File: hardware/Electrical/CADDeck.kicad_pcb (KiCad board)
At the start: 2 copper layers, 129 x 82.1 mm, 44 parts, among them J1 Conn_01x05_Socket, J4 Conn_01x04_Socket, J5 Conn_01x10_Socket, Q1 2N2222, SW1 SW_Push, SW10 SW_Push, SW2 SW_Push, SW3 SW_Push, SW4 SW_Push, SW5 SW_Push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

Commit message: Platine Optimiert
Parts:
- moved R11 97.1 mm to (87.9, 92.5)
- moved R12 81.9 mm to (87.9, 90.6), turned to 0 degrees
- renumbered J1 to J1_Knob, J4 to J4_Joystick, J5 to J5_WT32_SC01
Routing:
- net Net-(J5-Pin_10): track 123.8 -> 131.4 mm
- net Net-(J5-Pin_8): track 119.7 -> 126.0 mm
- net Net-(U1-P05): track 58.0 -> 63.6 mm
- net +3.3V: track 344.0 -> 346.0 mm
- net Net-(J5-Pin_7): track 131.7 -> 132.7 mm
- net Net-(J1-Pin_3): track 108.2 -> 107.3 mm
- net Net-(U1-P11): track 91.6 -> 92.3 mm
- net Net-(J4-Pin_4): track 113.2 -> 112.6 mm
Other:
- board size 129 x 82.1 mm -> 129 x 82.5 mm
- board text added: "+"
- board text added: "CADDeck by Andrew Fernie"
- board text added: "IO25"
- board text added: "IO27"
- board text added: "IO32"
- board text added: "IO33"
- board text added: "IO34"
- board text added: "IO35"
- board text added: "Rot"
- board text added: "SCL"
- board text added: "SDA"
- board text added: "TP223"
- board text added: "Vers. 2.0"
- board text added: "X-Joy"
- board text added: "Y-Joy"
- board text added: "Zoom"
- board text removed: "Andrew Fernie"
- board text removed: "LED"

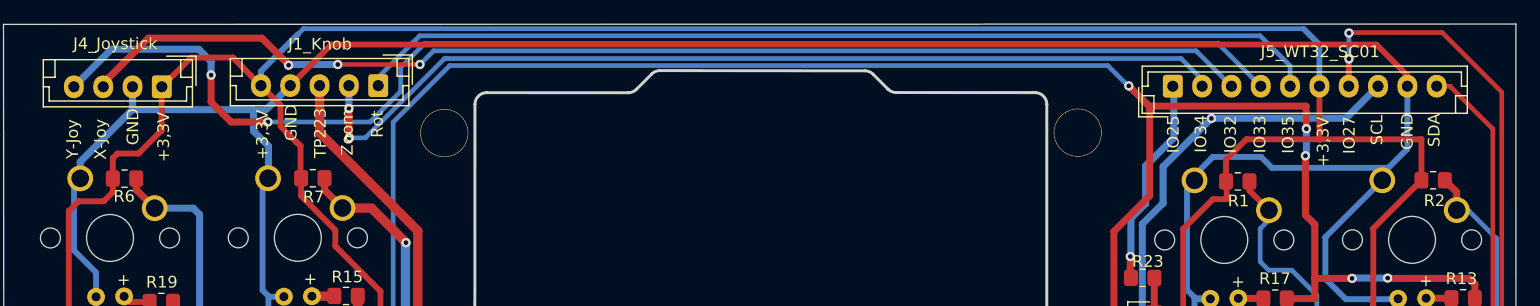
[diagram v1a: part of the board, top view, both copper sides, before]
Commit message: Stecker verrückt
um mehr Platz an den Abstandshaltern zu bekommen.
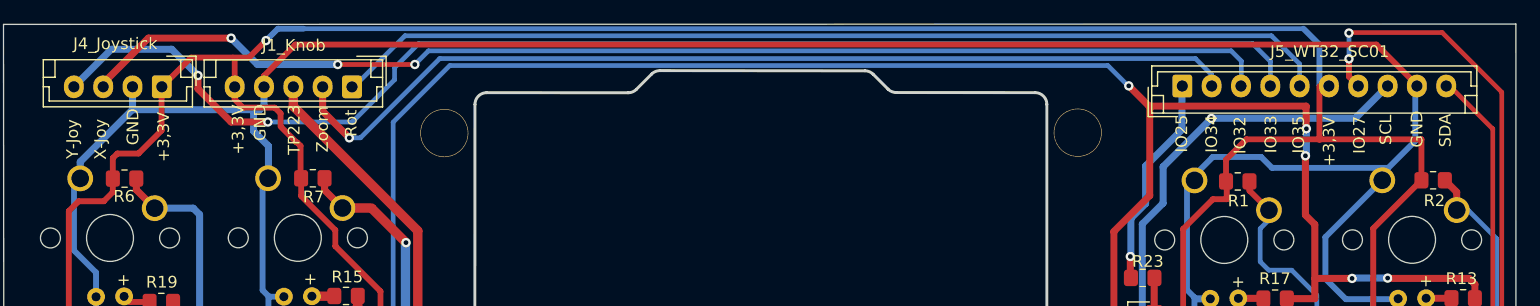
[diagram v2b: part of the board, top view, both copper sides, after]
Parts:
- moved J1_Knob 2.24 mm to (64.8, 22.0)
- moved J5_WT32_SC01 0.81 mm to (135.6, 22.0)
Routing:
- net Net-(J1-Pin_1): track 82.0 -> 85.5 mm
- net GND: track 359.0 -> 361.2 mm
- net +3.3V: track 346.0 -> 348.1 mm, vias 2 -> 3
- net Net-(J4-Pin_3): track 100.8 -> 102.9 mm
- net Net-(J1-Pin_2): track 81.3 -> 83.2 mm, vias 2 -> 1
- net Net-(J5-Pin_10): track 131.4 -> 130.2 mm
- net Net-(J5-Pin_8): track 126.0 -> 126.9 mm
- net Net-(J1-Pin_3): track 107.3 -> 108.1 mm

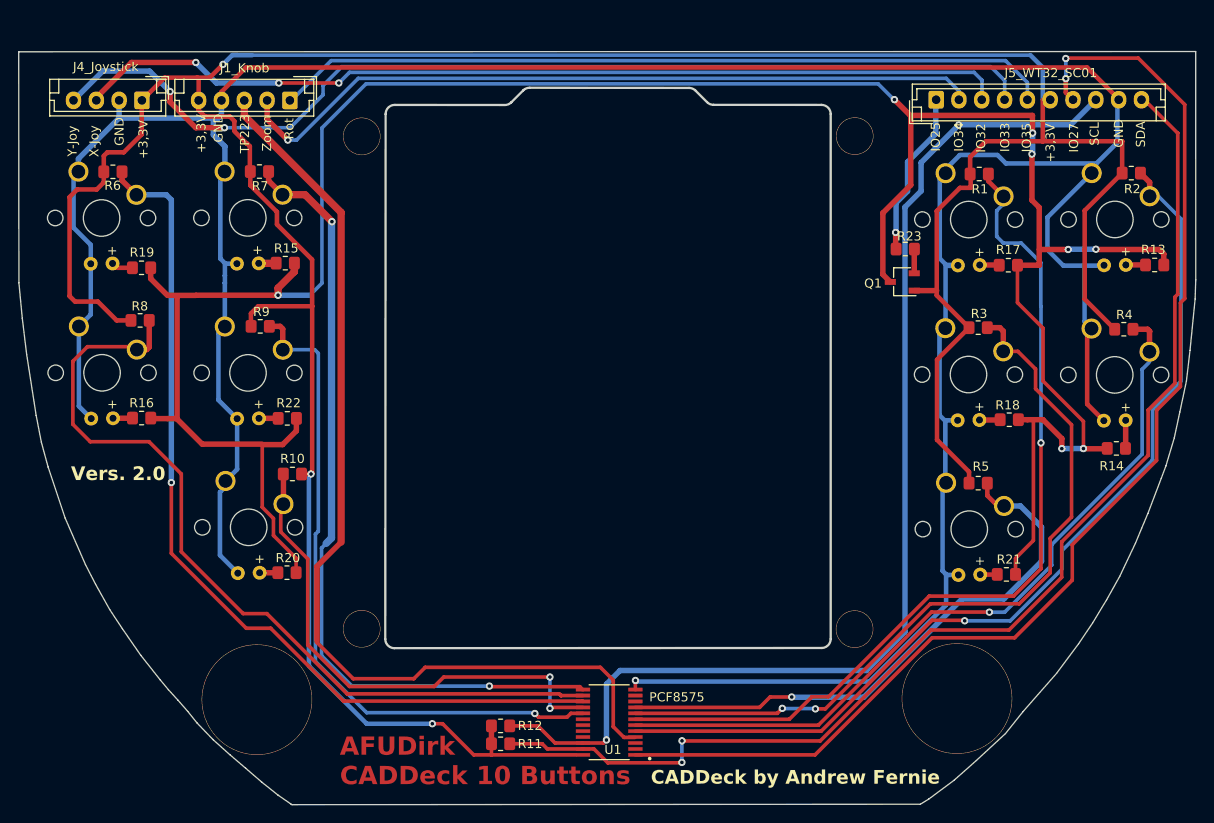
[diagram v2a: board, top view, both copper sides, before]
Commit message: Neue Platine in 3D Modell eingefügt
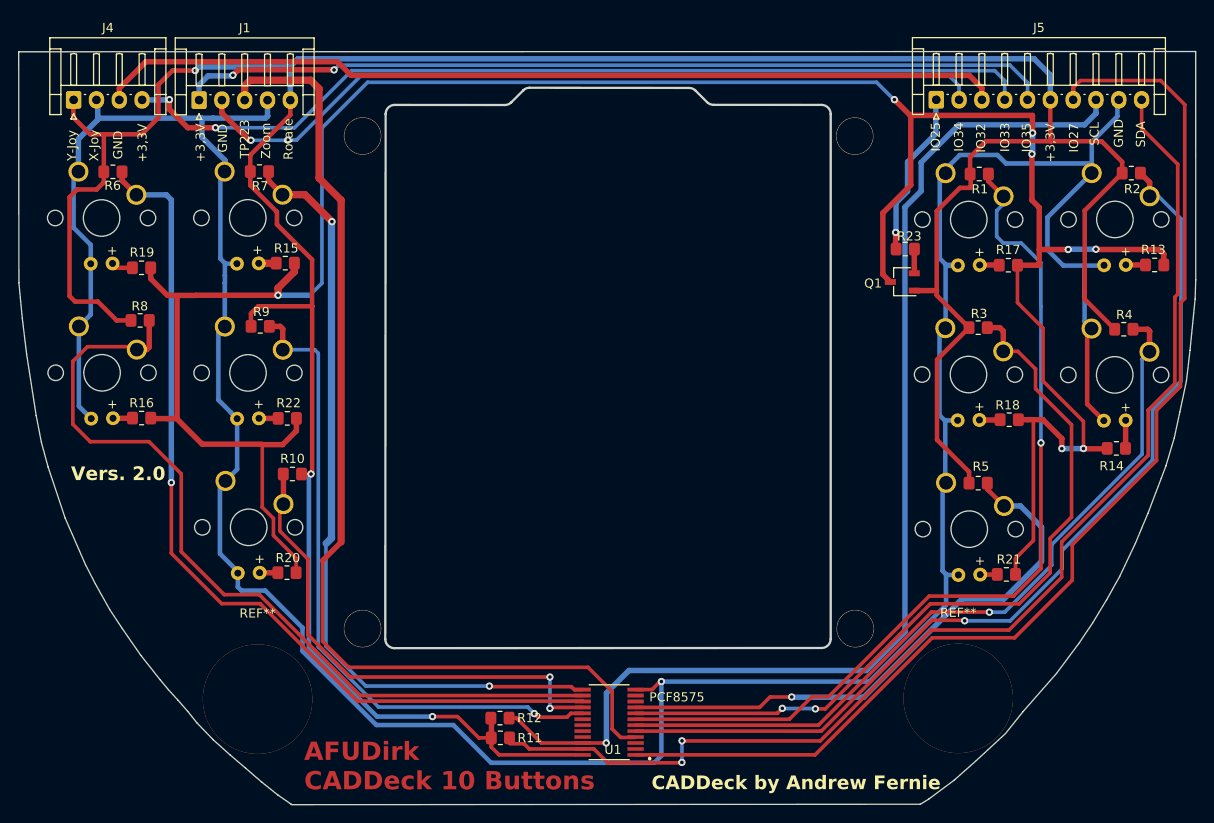
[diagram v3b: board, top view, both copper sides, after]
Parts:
- removed ? (x5): , 
- removed J1_Knob: Conn_01x05_Socket, Connector_JST:JST_EH_B5B-EH-A_1x05_P2.50mm_Vertical
- removed J4_Joystick: Conn_01x04_Socket, Connector_JST:JST_EH_B4B-EH-A_1x04_P2.50mm_Vertical
- removed J5_WT32_SC01: Conn_01x10_Socket, Connector_JST:JST_EH_B10B-EH-A_1x10_P2.50mm_Vertical
- added H2: Bohrung Joy, MountingHole:MountingHole_3.2mm_M3_DIN965, F.Cu at (72.8, 25.9)
- added H2: Bohrung Joy, MountingHole:MountingHole_3.2mm_M3_DIN965, F.Cu at (72.8, 79.9)
- added H2: Bohrung Joy, MountingHole:MountingHole_3.2mm_M3_DIN965, F.Cu at (126.8, 79.9)
- added J1: Conn_01x05_Socket, Connector_JST:JST_EH_S5B-EH_1x05_P2.50mm_Horizontal, F.Cu at (54.9, 22.0)
- added J4: Conn_01x04_Socket, Connector_JST:JST_EH_S4B-EH_1x04_P2.50mm_Horizontal, F.Cu at (41.1, 22.0)
- added J5: Conn_01x10_Socket, Connector_JST:JST_EH_S10B-EH_1x10_P2.50mm_Horizontal, F.Cu at (135.6, 22.0)
- added REF**: MountingHole_12,0mm, Joystick:MountingHole_12.0mm, F.Cu at (61.3, 87.6)
- added REF**: MountingHole_12,0mm, Joystick:MountingHole_12.0mm, F.Cu at (138.0, 87.6)
- moved R12 0.86 mm to (87.8, 89.7)
- moved R11 0.65 mm to (87.9, 91.9)
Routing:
- net GND: track 361.2 -> 335.1 mm
- net Net-(J4-Pin_4): track 112.7 -> 101.6 mm
- net Net-(J1-Pin_1): track 85.5 -> 96.0 mm, vias 0 -> 2
- net Net-(J1-Pin_3): track 108.1 -> 113.9 mm
- net Net-(J1-Pin_2): track 83.2 -> 88.4 mm, vias 1 -> 2
- net Net-(J5-Pin_7): track 133.0 -> 128.0 mm, vias 2 -> 0
- net +3.3V: track 348.1 -> 352.8 mm
- net Net-(J4-Pin_3): track 102.9 -> 99.5 mm, vias 3 -> 0
- net Net-(U1-P13): track 56.0 -> 54.6 mm
- net Net-(U1-P10): track 88.0 -> 86.7 mm
- net Net-(J5-Pin_8): track 126.9 -> 127.8 mm, vias 2 -> 1
- net Net-(U1-P14): track 73.0 -> 72.5 mm
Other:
- board text added: "Rotate"
- board text removed: "Rot"

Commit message: Bilder aktualisiert
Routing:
- net GND: track 335.1 -> 334.0 mm

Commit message: Massefläche hinzugefügt
Massefläche hinzugefügt
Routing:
- added copper zone on B.Cu, net GND
- added copper zone on F.Cu, net GND
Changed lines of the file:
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@@
     (tags "mounting hole 8.4mm no annular m8")
     (attr exclude_from_pos_files exclude_from_bom)
-    (fp_text reference "REF**" (at 0 -9.4) (layer "F.SilkS")
+    (fp_text reference "REF**" (at 0 -9.4) (layer "F.SilkS") hide
         (effects (font (size 1 1) (thickness 0.15)))
     )
@@
         (effects (font (size 1 1) (thickness 0.15)))
     )
-    (fp_circle (center 0 0) (end 8.4 0)
-      (stroke (width 0.15) (type solid)) (fill none) (layer "Cmts.User"))
-    (fp_circle (center 0 0) (end 8.65 0)
-      (stroke (width 0.05) (type solid)) (fill none) (layer "F.CrtYd"))
     (pad "" thru_hole circle (at 0 0) (size 12 12) (drill 12) (layers "*.Cu" "*.Mask"))
   )
@@
     (fp_line (start 10 1.5) (end 9 1.5)
       (stroke (width 0.1) (type solid)) (layer "F.Fab"))
-    (pad "1" thru_hole roundrect (at 0 0) (size 1.7 1.95) (drill 0.95) (layers "*.Cu" "*.Mask") (roundrect_rratio 0.147059)
+    (pad "1" thru_hole roundrect (at 0 0) (size 1.7 1.95) (drill 0.95) (layers "*.Cu" "*.Mask") (roundrect_rratio 0.1470588235)
       (net 1 "+3.3V") (pinfunction "Pin_1") (pintype "passive"))
     (pad "2" thru_hole oval (at 2.5 0) (size 1.7 1.95) (drill 0.95) (layers "*.Cu" "*.Mask")
@@
     (fp_line (start 25 1.5) (end 24 1.5)
       (stroke (width 0.1) (type solid)) (layer "F.Fab"))
-    (pad "1" thru_hole roundrect (at 0 0) (size 1.7 1.95) (drill 0.95) (layers "*.Cu" "*.Mask") (roundrect_rratio 0.147059)
+    (pad "1" thru_hole roundrect (at 0 0) (size 1.7 1.95) (drill 0.95) (layers "*.Cu" "*.Mask") (roundrect_rratio 0.1470588235)
       (net 30 "Net-(J5-Pin_1)") (pinfunction "Pin_1") (pintype "passive"))
     (pad "2" thru_hole oval (at 2.5 0) (size 1.7 1.95) (drill 0.95) (layers "*.Cu" "*.Mask")
@@
     (tags "mounting hole 12,0mm")
     (attr exclude_from_pos_files exclude_from_bom)
-    (fp_text reference "REF**" (at 0 -9.4) (layer "F.SilkS")
-        (effects (font (size 1 1) (thickness 0.15)))
-    )
-    (fp_text value "MountingHole_12,0mm" (at 0 9.4) (layer "F.Fab")
+    (fp_text reference "REF**" (at 0 -9.4) (layer "F.SilkS") hide
+        (effects (font (size 1 1) (thickness 0.15)))
+    )
+    (fp_text value "MountingHole_12,0mm" (at 0 9.4) (layer "F.Fab") hide
         (effects (font (size 1 1) (thickness 0.15)))
     )
@@
         (effects (font (size 1 1) (thickness 0.15)))
     )
-    (fp_circle (center 0 0) (end 8.4 0)
-      (stroke (width 0.15) (type solid)) (fill none) (layer "Cmts.User"))
-    (fp_circle (center 0 0) (end 8.65 0)
-      (stroke (width 0.05) (type solid)) (fill none) (layer "F.CrtYd"))
     (pad "" thru_hole circle (at 0 0) (size 12 12) (drill 12) (layers "*.Cu" "*.Mask"))
   )
@@
     (fp_line (start 12.5 1.5) (end 11.5 1.5)
       (stroke (width 0.1) (type solid)) (layer "F.Fab"))
-    (pad "1" thru_hole roundrect (at 0 0) (size 1.7 1.95) (drill 0.95) (layers "*.Cu" "*.Mask") (roundrect_rratio 0.147059)
+    (pad "1" thru_hole roundrect (at 0 0) (size 1.7 1.95) (drill 0.95) (layers "*.Cu" "*.Mask") (roundrect_rratio 0.1470588235)
       (net 3 "Net-(J1-Pin_1)") (pinfunction "Pin_1") (pintype "passive"))
     (pad "2" thru_hole oval (at 2.5 0) (size 1.7 1.95) (drill 0.95) (layers "*.Cu" "*.Mask")
@@
   (segment (start 63.509 43.381) (end 66.999 43.381) (width 0.6) (layer "B.Cu") (net 41))
   (segment (start 150.114 38.341) (end 153.118 38.341) (width 0.6) (layer "B.Cu") (net 41))
+  (zone (net 2) (net_name "GND") (layers "F&B.Cu") (hatch edge 0.5)
+    (connect_pads (clearance 0.5))
+    (min_thickness 0.25) (filled_areas_thickness no)
+    (fill yes (thermal_gap 0.5) (thermal_bridge_width 0.5))
+    (polygon
+      (pts
+        (xy 35.477578 17.037229)
+        (xy 164.035578 16.833671)
+        (xy 164.004578 42.386671)
+        (xy 163.918578 44.147671)
+        (xy 163.646578 46.595671)
+        (xy 163.532578 47.955671)
+        (xy 163.228578 50.771671)
+        (xy 163.013578 52.704671)
+        (xy 162.369578 55.782671)
+        (xy 161.756578 58.581671)
+        (xy 160.811578 62.024671)
+        (xy 159.394578 65.569671)
+        (xy 158.280578 68.539671)
+        (xy 156.828578 71.813671)
+        (xy 155.444578 74.648671)
+        (xy 153.993578 77.180671)
+        (xy 152.858578 79.041671)
+        (xy 150.967578 81.831671)
+        (xy 148.616578 84.989671)
+        (xy 146.264578 87.687671)
+        (xy 143.751578 90.661671)
+        (xy 141.751578 92.728671)
+        (xy 138.112578 96.232671)
+        (xy 134.563578 98.703671)
+        (xy 133.938578 99.159671)
+        (xy 65.113578 99.248671)
+        (xy 63.465578 98.132671)
+        (xy 61.106578 96.230671)
+        (xy 58.063578 93.643671)
+        (xy 54.577578 90.379671)
+        (xy 50.266578 85.145671)
+        (xy 47.038578 80.880671)
+        (xy 44.747578 77.331671)
+        (xy 42.680578 73.602671)
+        (xy 41.108578 69.873671)
+        (xy 39.673578 66.264671)
+        (xy 38.458578 62.484671)
+        (xy 37.277578 57.893671)
+        (xy 36.429578 52.489671)
+        (xy 35.849578 48.751671)
+        (xy 35.354578 43.947671)
+        (xy 35.226578 42.058671)
+        (xy 35.197578 41.127671)
+        (xy 35.207648 17.03619)
+        (xy 35.237648 17.03619)
+        (xy 35.393648 17.03619)
+      )
+    )
+  )
   (group "" (id a9e57f5b-5234-4a0e-aed1-ec53447751c9)
     (members

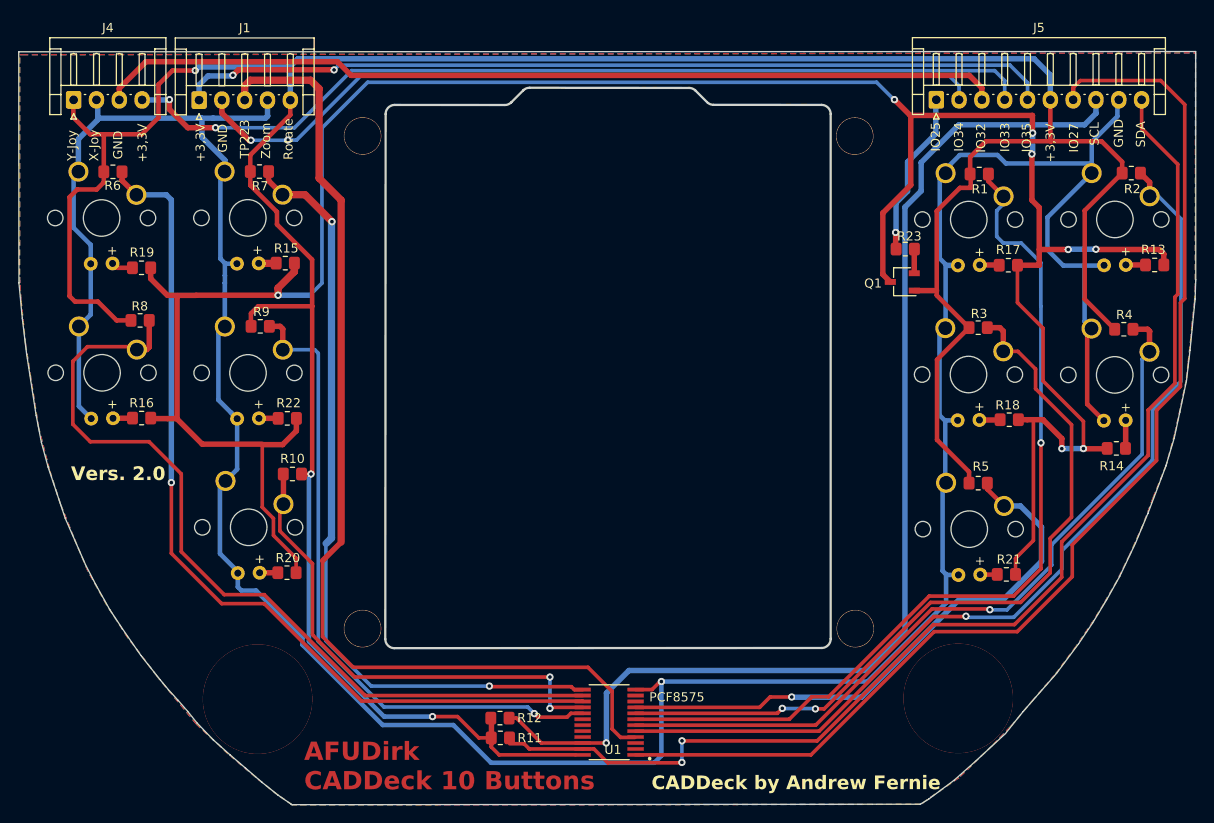
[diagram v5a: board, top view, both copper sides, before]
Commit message: Kleine Korrekturen
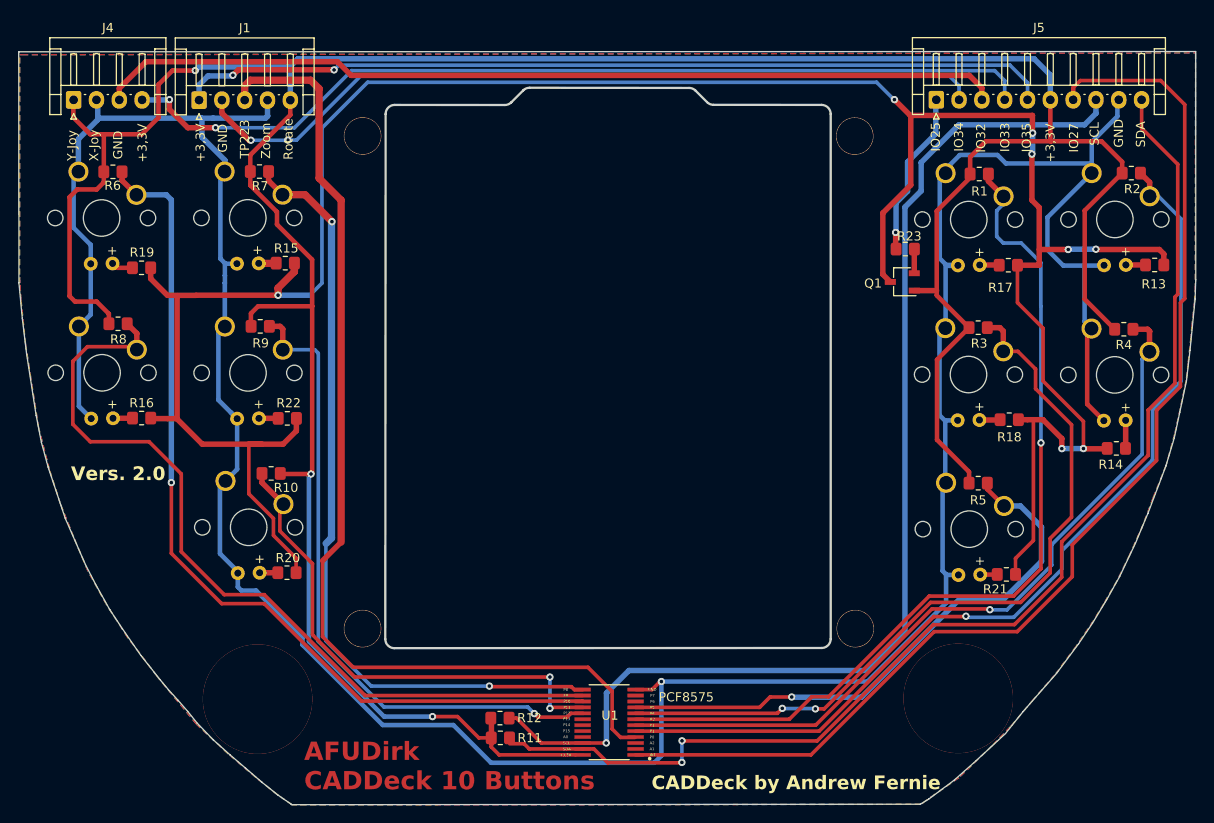
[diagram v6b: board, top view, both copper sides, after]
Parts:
- moved R8 2.45 mm to (46.0, 46.5)
- moved R10 2.33 mm to (62.8, 62.9)
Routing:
- net Net-(Q1-C): track 280.6 -> 284.1 mm
- net Net-(U1-P11): track 92.3 -> 91.1 mm
- net Net-(U1-P13): track 54.3 -> 55.3 mm
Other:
- board text added: "A0"
- board text added: "A1"
- board text added: "A2"
- board text added: "INT"
- board text added: "P0"
- board text added: "P1"
- board text added: "P10"
- board text added: "P11"
- board text added: "P12"
- board text added: "P13"
- board text added: "P14"
- board text added: "P15"
- board text added: "P2"
- board text added: "P3"
- board text added: "P4"
- board text added: "P5"
- board text added: "P6"
- board text added: "P7"
- board text added: "P8"
- board text added: "P9"

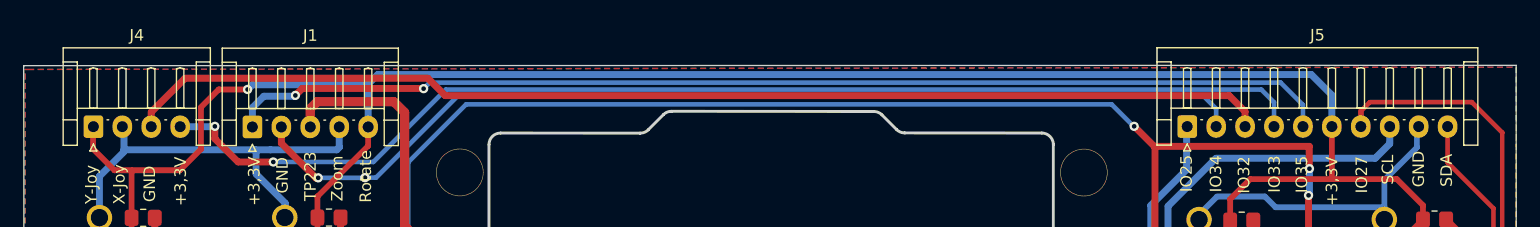
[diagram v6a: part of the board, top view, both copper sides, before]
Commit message: Footprints geändert
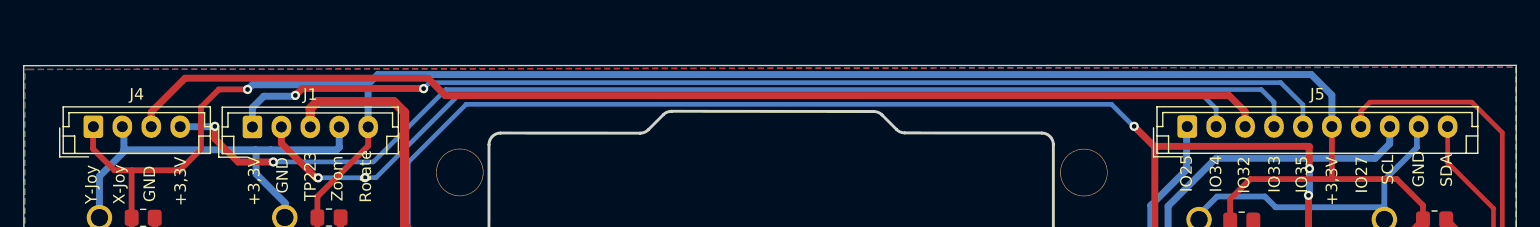
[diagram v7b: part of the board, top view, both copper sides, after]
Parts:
- J1: footprint Connector_JST:JST_EH_S5B-EH_1x05_P2.50mm_Horizontal -> Connector_JST:JST_EH_B5B-EH-A_1x05_P2.50mm_Vertical
- J4: footprint Connector_JST:JST_EH_S4B-EH_1x04_P2.50mm_Horizontal -> Connector_JST:JST_EH_B4B-EH-A_1x04_P2.50mm_Vertical
- J5: footprint Connector_JST:JST_EH_S10B-EH_1x10_P2.50mm_Horizontal -> Connector_JST:JST_EH_B10B-EH-A_1x10_P2.50mm_Vertical
